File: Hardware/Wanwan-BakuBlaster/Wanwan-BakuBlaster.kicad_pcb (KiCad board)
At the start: 2 copper layers, 96 x 60.5 mm, 70 parts, among them Q1 BSS138, U1 RP2040-Zero, U2 PT8211, U3 TLV2372

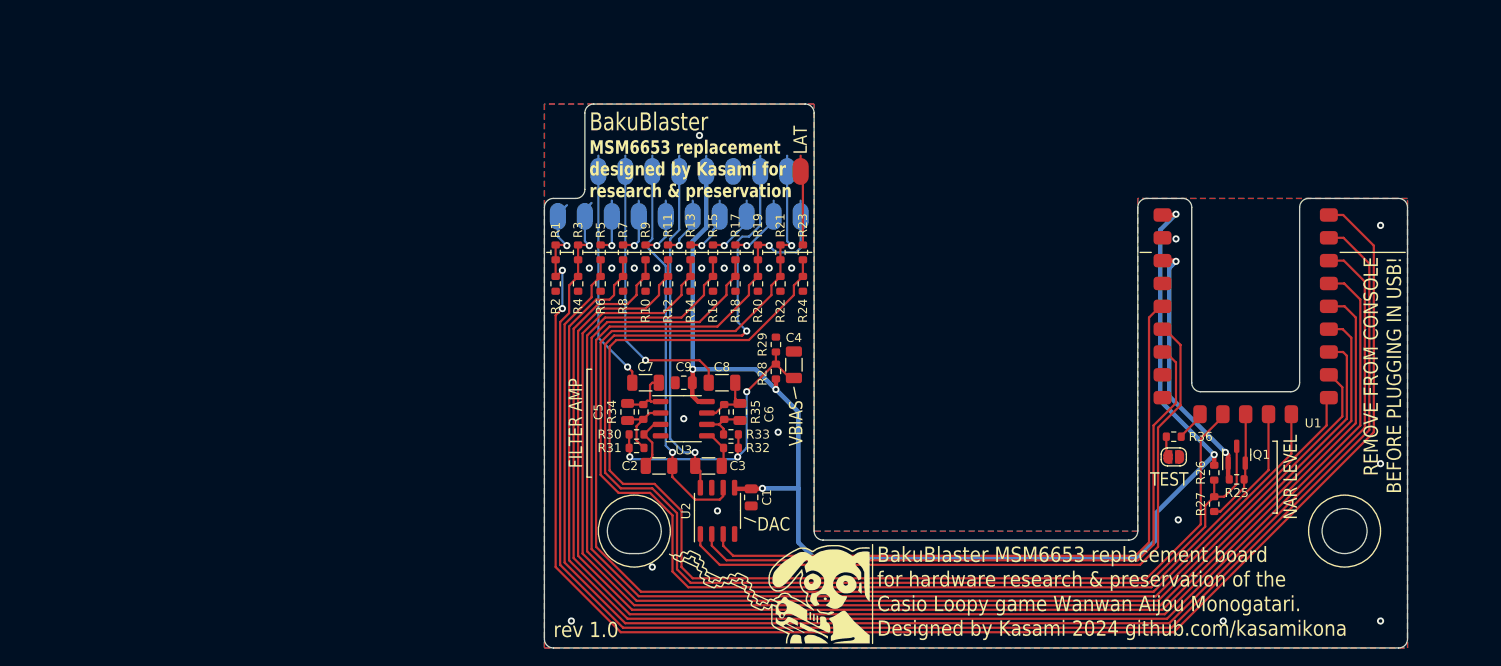
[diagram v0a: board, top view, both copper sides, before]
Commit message: Update clearances
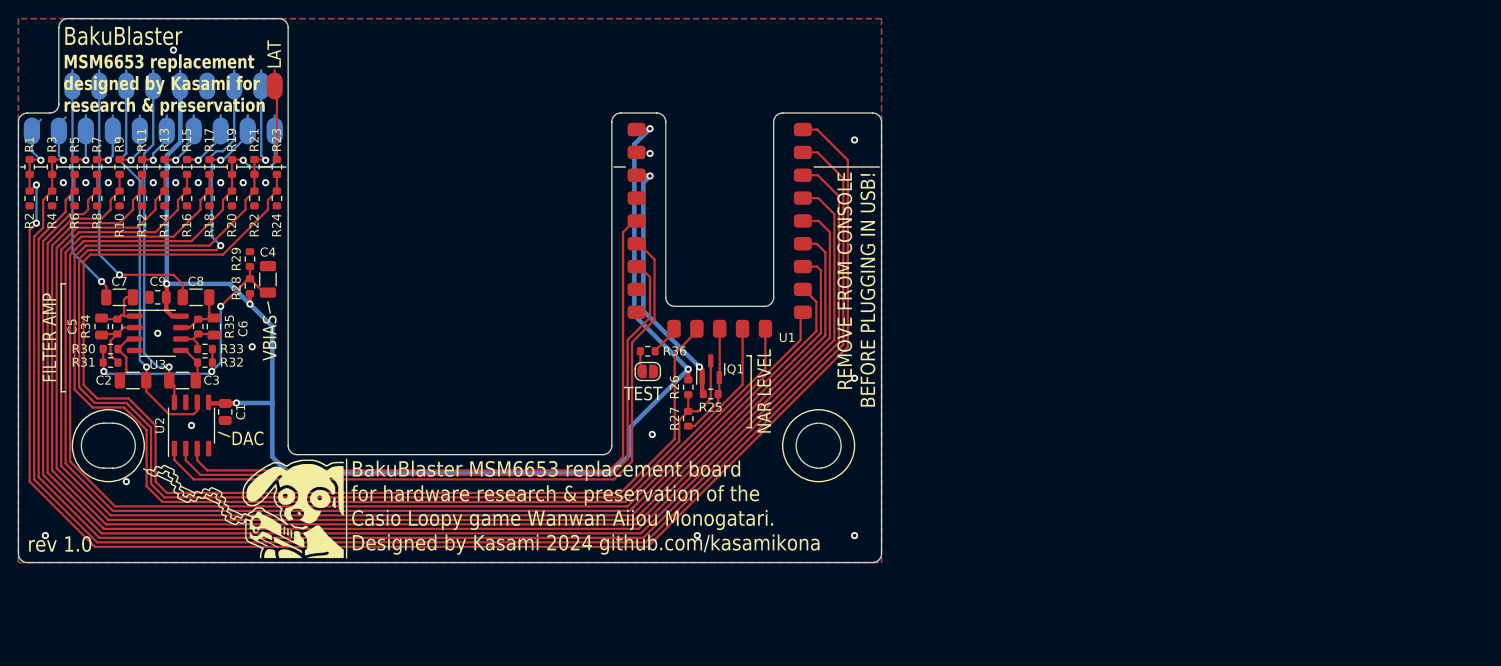
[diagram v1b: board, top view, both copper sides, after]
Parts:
- moved C1 59.3 mm to (38.0, 57.8)
- moved C2 59.3 mm to (27.8, 54.2)
- moved C3 59.3 mm to (33.2, 54.2)
- moved C4 59.3 mm to (42.8, 43.0)
- moved C5 59.3 mm to (24.2, 48.2)
- moved C6 59.3 mm to (36.8, 48.2)
- moved C7 59.3 mm to (26.2, 45.0)
- moved C8 59.3 mm to (34.8, 45.0)
- moved C9 59.3 mm to (30.5, 45.0)
- moved G*** 59.3 mm to (40.0, 68.5)
- moved JP1 59.3 mm to (85.0, 53.2)
- moved Q1 59.3 mm to (92.0, 53.0)
- moved R1 59.3 mm to (16.2, 30.5)
- moved R10 59.3 mm to (26.2, 34.0)
- moved R11 59.3 mm to (28.8, 30.5)
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
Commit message: Update hardware stuff
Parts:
- R1, R19, R21, R27, R3: value 1K -> DNP
- R25: value 2K2 -> DNP
